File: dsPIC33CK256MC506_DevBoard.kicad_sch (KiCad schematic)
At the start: 31 parts, among them J1 ICSP, J2 Pins_01_to_16, J3 Conn_02x06_Odd_Even, J4 Conn_01x02, J5 Conn_02x02_Odd_Even, J6 Pins_01_to_16, J7 Pins_17_to_32, Q1 DTC143Z, Q2 DTC143Z, Q3 DTC143Z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

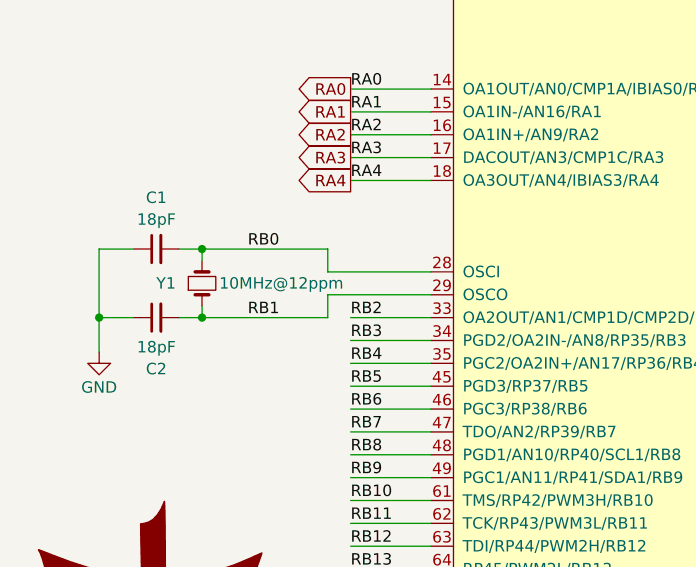
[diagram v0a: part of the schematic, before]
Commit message: Updated documentation and component values
 - Schematic for analyzing
 - Schematic for printing
 - Interactive BOM for assembly
 - Updated component values
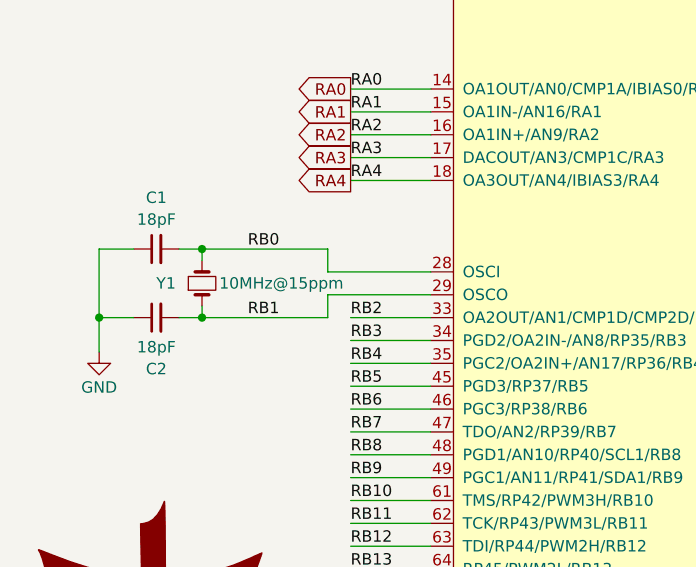
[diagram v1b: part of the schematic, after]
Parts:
- C1, C2: MOUSER Part (none) -> 791-0805N180J500CT
- C3, C4, C5, C6: MOUSER Part (none) -> Generic 0603 ceramic capacitor
- D1: MOUSER Part (none) -> Generic 0805 RED SMD LED
- D2, D3, D4: MOUSER Part (none) -> Generic 0805 AMBAR SMD LED
- J1, J4: MOUSER Part (none) -> Geneeric 2.54mm(100 mil) single line male pin header
- J2, J3, J5, J6, J7: MOUSER Part (none) -> Geneeric 2.54mm(100 mil) dual line male pin header
- Q1, Q2, Q3, Q4: MOUSER Part (none) -> 771-PDTC143ZTT/R
- R1, R2, R3, R4, R5, R6, R7: MOUSER Part (none) -> Generic 0805 SMD resistor
- SW1: MOUSER Part (none) -> 3x6x2.5mm SMD push button
- U1: MOUSER Part (none) -> 579-D33CK256MC506IPT
- Y1: value 10MHz@12ppm -> 10MHz@15ppm; MOUSER Part (none) -> 669-E1SHA18-10T
